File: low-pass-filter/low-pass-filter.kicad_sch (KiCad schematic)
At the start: 40 parts, among them J1 Power, J2 Power, J3 Pot, J4 CV, J5 Output, J6 Pot, J7 Input, J9 Pot, Q1 PNP, Q2 PNP, U1 LM13700, U2 TL074

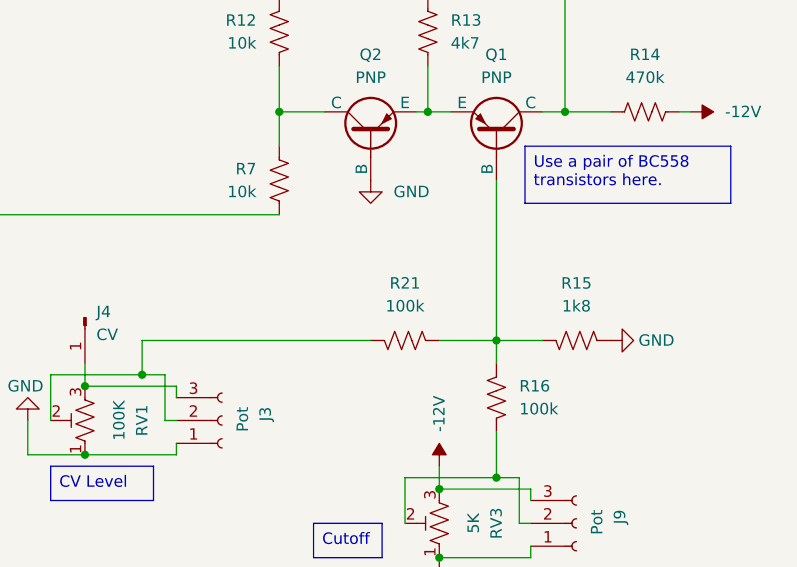
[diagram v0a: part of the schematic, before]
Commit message: Envelope generator
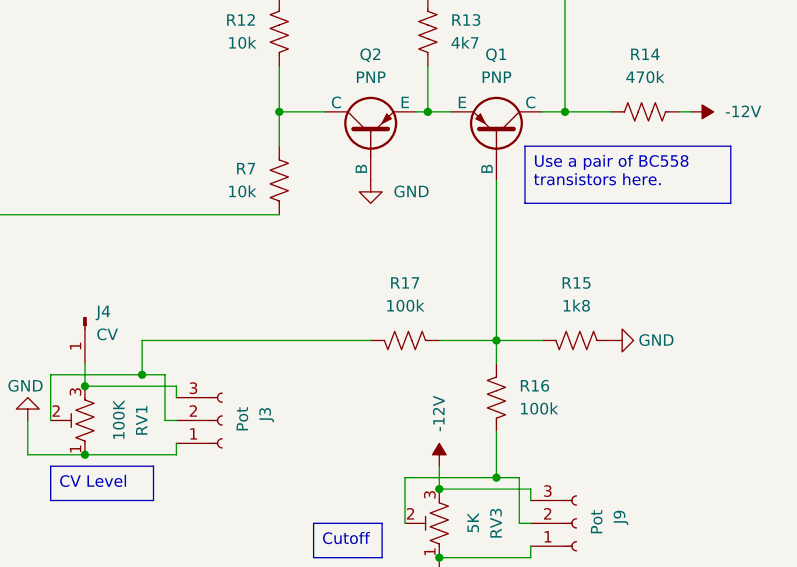
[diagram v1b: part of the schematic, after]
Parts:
- C1, C2, C3, C4, C5, C6: footprint Capacitor_THT:C_Disc_D5.0mm_W2.5mm_P2.50mm -> Capacitor_THT:C_Disc_D4.3mm_W1.9mm_P5.00mm
- renumbered R21 to R17
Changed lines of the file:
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@@
 			)
 		)
-		(property "Footprint" "Capacitor_THT:C_Disc_D5.0mm_W2.5mm_P2.50mm"
+		(property "Footprint" "Capacitor_THT:C_Disc_D4.3mm_W1.9mm_P5.00mm"
 			(at 31.75 120.65 0)
 			(effects
@@
 			)
 		)
-		(property "Footprint" "Capacitor_THT:C_Disc_D5.0mm_W2.5mm_P2.50mm"
+		(property "Footprint" "Capacitor_THT:C_Disc_D4.3mm_W1.9mm_P5.00mm"
 			(at 41.91 120.65 0)
 			(effects
@@
 			)
 		)
-		(property "Footprint" "Capacitor_THT:C_Disc_D5.0mm_W2.5mm_P2.50mm"
+		(property "Footprint" "Capacitor_THT:C_Disc_D4.3mm_W1.9mm_P5.00mm"
 			(at 251.46 92.71 0)
 			(effects
@@
 			)
 		)
-		(property "Footprint" "Capacitor_THT:C_Disc_D5.0mm_W2.5mm_P2.50mm"
+		(property "Footprint" "Capacitor_THT:C_Disc_D4.3mm_W1.9mm_P5.00mm"
 			(at 245.11 38.1 0)
 			(effects
@@
 		(dnp no)
 		(fields_autoplaced yes)
-		(property "Reference" "R21"
+		(property "Reference" "R17"
 			(at 241.3 132.08 90)
 			(effects
@@
 			(project "low-pass-filter"
 				(path "/8654abdc-c56c-4f7a-a1d7-4eb247d6aa0a"
-					(reference "R21")
+					(reference "R17")
 					(unit 1)
 				)
@@
 			)
 		)
-		(property "Footprint" "Capacitor_THT:C_Disc_D5.0mm_W2.5mm_P2.50mm"
+		(property "Footprint" "Capacitor_THT:C_Disc_D4.3mm_W1.9mm_P5.00mm"
 			(at 153.67 41.91 0)
 			(effects
@@
 			)
 		)
-		(property "Footprint" "Capacitor_THT:C_Disc_D5.0mm_W2.5mm_P2.50mm"
+		(property "Footprint" "Capacitor_THT:C_Disc_D4.3mm_W1.9mm_P5.00mm"
 			(at 138.43 105.41 0)
 			(effects

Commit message: Various improvements
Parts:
- added C7, C8: 100nf, Capacitor_THT:C_Disc_D4.3mm_W1.9mm_P5.00mm, symbol Device:C_Small
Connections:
- net -12V: now also C2.1, C7.2; no longer C1.1
- net 12V: now also C1.2, C8.1; no longer C2.2
- net GND: now also C1.1, C2.2, C7.1, C8.2; no longer C1.2, C2.1
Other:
- moved on the sheet: C1, C2, U1B, U1D, U1E, U2E

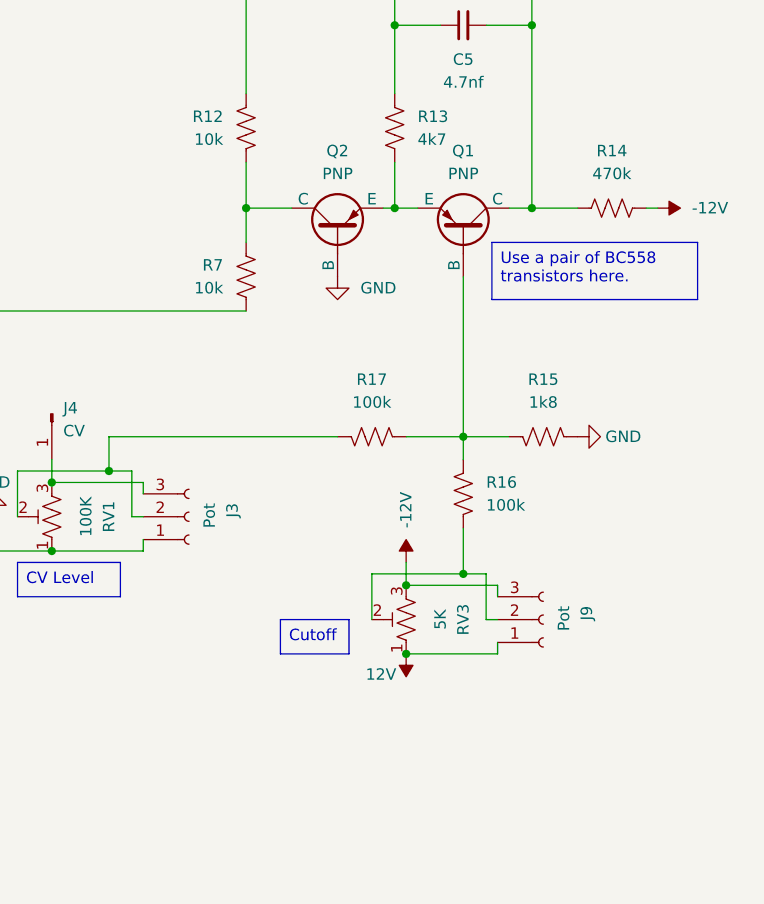
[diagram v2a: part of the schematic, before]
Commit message: Update low-pass filter
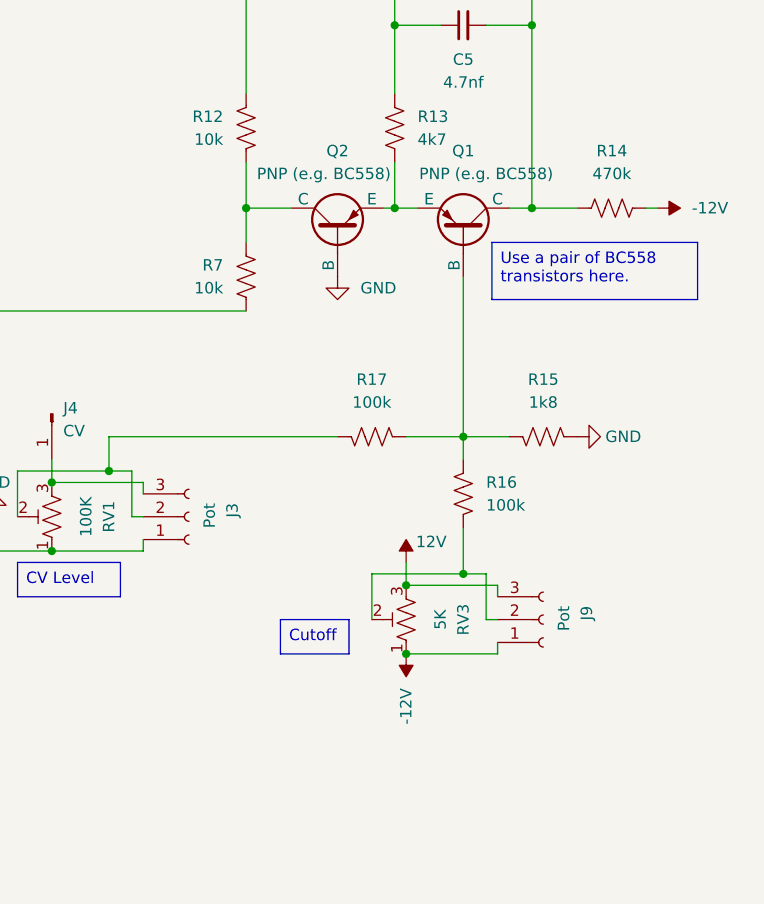
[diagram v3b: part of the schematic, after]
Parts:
- Q1, Q2: value PNP -> PNP (e.g. BC558)
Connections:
- net -12V: now also J9.1 (Pin_1), RV3.1; no longer J9.3 (Pin_3), RV3.3
- net 12V: now also J9.3 (Pin_3), RV3.3; no longer J9.1 (Pin_1), RV3.1
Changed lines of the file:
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@@
 	)
 	(junction
-		(at 245.11 162.56)
-		(diameter 0)
-		(color 0 0 0 0)
-	)
-	(junction
 		(at 212.09 142.24)
 		(diameter 0)
@@
 	)
 	(junction
+		(at 245.11 162.56)
+		(diameter 0)
+		(color 0 0 0 0)
+	)
+	(junction
 		(at 191.77 41.91)
 		(diameter 0)
@@
 		(on_board yes)
 		(dnp no)
-		(fields_autoplaced yes)
 		(property "Reference" "Q2"
 			(at 237.49 106.68 90)
@@
 			)
 		)
-		(property "Value" "PNP"
-			(at 237.49 109.22 90)
+		(property "Value" "PNP (e.g. BC558)"
+			(at 235.966 109.22 90)
 			(effects
 				(font
@@
 	(symbol
 		(lib_id "power:-12V")
-		(at 245.11 162.56 0)
-		(mirror x)
+		(at 245.11 152.4 0)
+		(mirror y)
 		(unit 1)
 		(exclude_from_sim no)
@@
 		(dnp no)
 		(property "Reference" "#PWR025"
-			(at 245.11 158.75 0)
+			(at 245.11 156.21 0)
 			(effects
 				(font
@@
 		)
 		(property "Value" "12V"
-			(at 242.316 164.846 0)
+			(at 247.904 150.114 0)
 			(effects
 				(font
@@
 		)
 		(property "Footprint" ""
-			(at 245.11 162.56 0)
+			(at 245.11 152.4 0)
 			(effects
 				(font
@@
 		)
 		(property "Datasheet" ""
-			(at 245.11 162.56 0)
+			(at 245.11 152.4 0)
 			(effects
 				(font
@@
 		)
 		(property "Description" "Power symbol creates a global label with name \"-12V\""
-			(at 245.11 162.56 0)
+			(at 245.11 152.4 0)
 			(effects
 				(font
@@
 	(symbol
 		(lib_id "power:-12V")
-		(at 245.11 152.4 0)
-		(mirror y)
+		(at 245.11 162.56 0)
+		(mirror x)
 		(unit 1)
 		(exclude_from_sim no)
@@
 		(dnp no)
 		(property "Reference" "#PWR022"
-			(at 245.11 149.86 0)
+			(at 245.11 165.1 0)
 			(effects
 				(font
@@
 		)
 		(property "Value" "-12V"
-			(at 245.11 148.59 90)
+			(at 245.11 166.37 90)
 			(effects
 				(font
@@
 		)
 		(property "Footprint" ""
-			(at 245.11 152.4 0)
+			(at 245.11 162.56 0)
 			(effects
 				(font
@@
 		)
 		(property "Datasheet" ""
-			(at 245.11 152.4 0)
+			(at 245.11 162.56 0)
 			(effects
 				(font
@@
 		)
 		(property "Description" ""
-			(at 245.11 152.4 0)
+			(at 245.11 162.56 0)
 			(effects
 				(font
@@
 		(on_board yes)
 		(dnp no)
-		(fields_autoplaced yes)
 		(property "Reference" "Q1"
 			(at 251.46 106.68 90)
@@
 			)
 		)
-		(property "Value" "PNP"
-			(at 251.46 109.22 90)
+		(property "Value" "PNP (e.g. BC558)"
+			(at 254 109.22 90)
 			(effects
 				(font

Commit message: Various fixes
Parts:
- added J8: Power, Connector_IDC:IDC-Header_2x03_P2.54mm_Vertical, symbol Connector_Generic:Conn_02x03_Odd_Even
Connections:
- net -12V: now also J8.2 (Pin_2)
- net 12V: now also J8.1 (Pin_1)
- net 5V: now also J8.5 (Pin_5)
- net GND: now also J8.3 (Pin_3), J8.4 (Pin_4)
- no-connect marks 8 -> 9

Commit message: Various improvements
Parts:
- R17: value 100k -> 24k
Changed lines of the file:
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@@
 		)
 	)
+	(text_box "R17 controls the maximum effect of CV. Reduce its resistance to increase the max CV effect."
+		(exclude_from_sim no)
+		(at 200.66 125.73 0)
+		(size 36.83 7.62)
+		(margins 0.9525 0.9525 0.9525 0.9525)
+		(stroke
+			(width 0)
+			(type solid)
+		)
+		(fill
+			(type none)
+		)
+		(effects
+			(font
+				(size 1.27 1.27)
+			)
+			(justify left top)
+		)
+	)
 	(junction
 		(at 116.84 68.58)
@@
 			)
 		)
-		(property "Value" "100k"
+		(property "Value" "24k"
 			(at 241.3 134.62 90)
 			(effects
